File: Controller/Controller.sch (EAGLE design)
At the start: 40 parts, among them Q1 16Mhz, Q2 DMMT5401, Q3 DMG2305UX

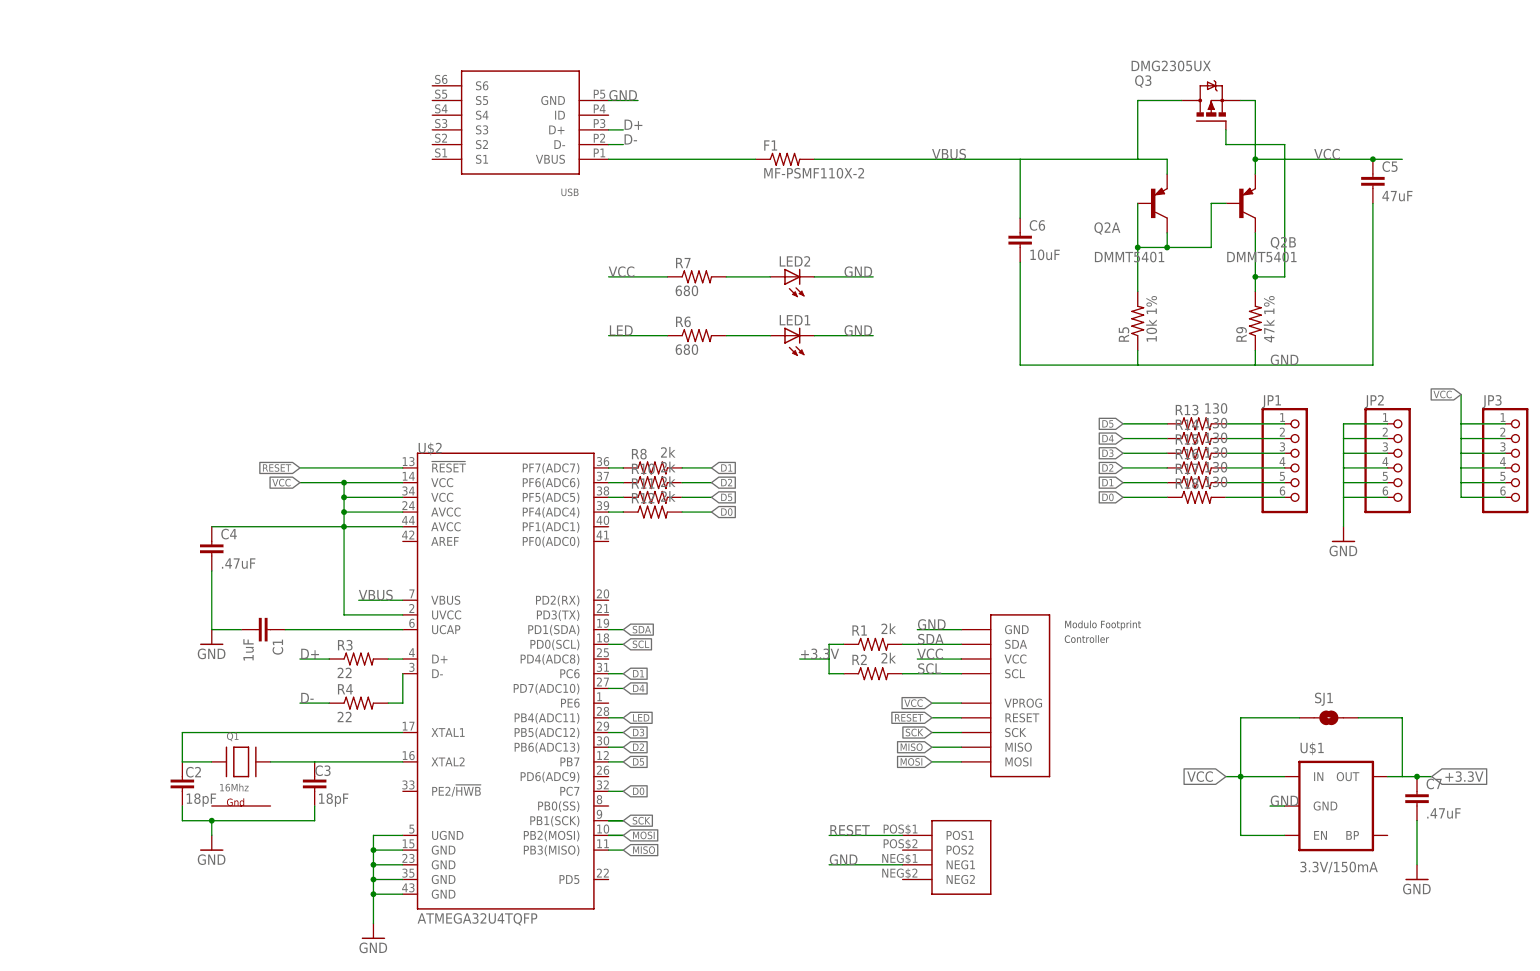
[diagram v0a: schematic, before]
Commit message: Renamed 32u4 to Controller
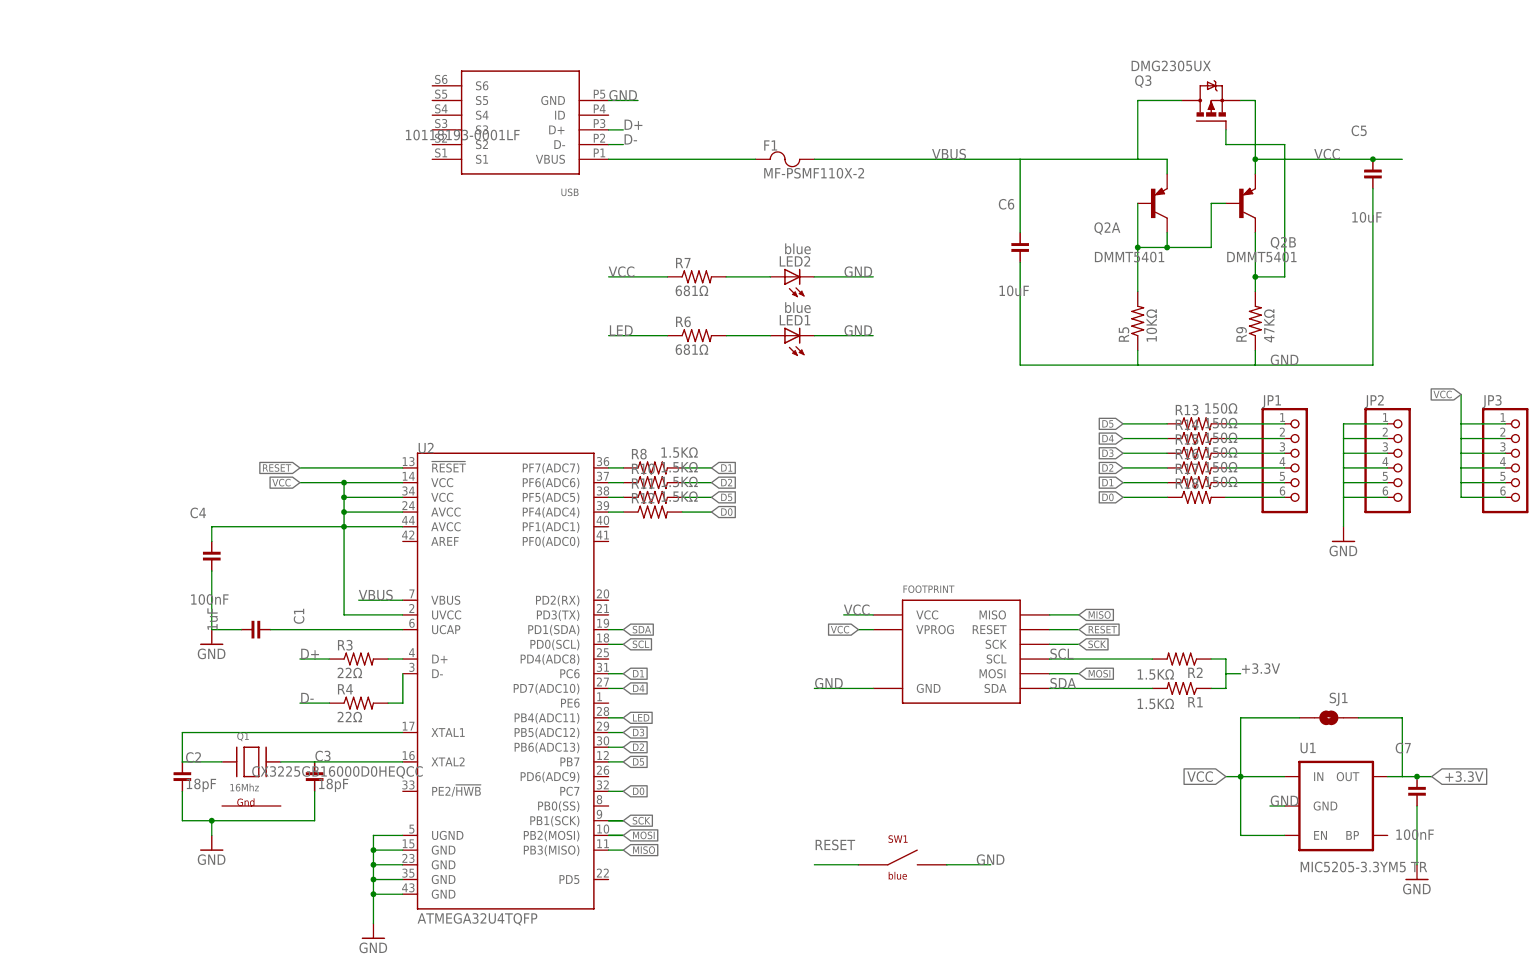
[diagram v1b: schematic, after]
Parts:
- removed U$1: 3.3V/150mA, SparkFun-PowerIC:V_REG_MIC52053.3V
- removed U$6: TACT-SWITCHBOURNS-7914J, IntegerLabs:TACT-SWITCHBOURNS-7914J
- added SW1: blue, Modulo:SWITCHBOURNS-7914J
- added U1: MIC5205-3.3YM5 TR, Modulo:VREG-MIC5205-3.3V
- C1: device SparkFun-Capacitors:CAP0805 -> Modulo:CAPACITOR-1UF
- C2, C3: device SparkFun-Capacitors:CAP0805 -> Modulo:CAPACITOR-18PF
- C4, C7: value .47uF -> 100nF; device SparkFun-Capacitors:CAP0805 -> Modulo:CAPACITOR-100NF
- C5: value 47uF -> 10uF; device SparkFun-Capacitors:CAP1206 -> Modulo:CAPACITOR-10UF
- C6: device SparkFun-Capacitors:CAP0805 -> Modulo:CAPACITOR-10UF
- F1: device SparkFun-Resistors:RESISTOR0805-RES -> Modulo:FUSE; PARTNUM (none) -> MF-PSFM110X-2
- FOOTPRINT: value Controller -> DEVICE-PCB-TABS; device IntegerLabs:FOOTPRINTFOOTPRINT-2 -> Modulo:DEVICE-PCB-TABS; BOARD Controller -> (none); VERSION v5 -> (none)
- JP1, JP2, JP3: PARTNUM (none) -> PREC006SAAN-RC
- LED1: value (none) -> blue; device adafruit:LEDCHIP-LED0805 -> Modulo:LED-0805-BLUE
- LED2: value (none) -> blue; device led:LEDCHIPLED_0805 -> Modulo:LED-0805-BLUE
- Q1: device adafruit:XTAL-4-3225 -> Modulo:CRYSTAL-NX3225; PARTNUM (none) -> CX3225GB16000D0HEQCC
- Q2: PARTNUM (none) -> DMMT5401
- Q3: PARTNUM (none) -> DMG2305UX
- R1, R10, R11, R12, R2, R8: value 2k -> 1.5KΩ; device SparkFun-Resistors:RESISTOR0805-RES -> Modulo:RESISTOR-1.5KΩ
- R13, R14, R15, R16, R17, R18: value 130 -> 150Ω; device SparkFun-Resistors:RESISTOR0805-RES -> Modulo:RESISTOR-150Ω
- R3, R4: value 22 -> 22Ω; device SparkFun-Resistors:RESISTOR0805-RES -> Modulo:RESISTOR-22Ω
- R5: value 10k 1% -> 10KΩ; device SparkFun-Passives:RESISTOR0805-RES -> Modulo:RESISTOR-10KΩ
- R6, R7: value 680 -> 681Ω; device SparkFun-Resistors:RESISTOR0805-RES -> Modulo:RESISTOR-681Ω
- R9: value 47k 1% -> 47KΩ; device SparkFun-Passives:RESISTOR0805-RES -> Modulo:RESISTOR-47KΩ
- SJ1: PARTNUM (none) -> EXCLUDE
- U2: PARTNUM (none) -> ATMEGA32U4TQFP
- U3: PARTNUM (none) -> 10118193-0001LF
- renumbered U$2 to U2, U$4 to U3
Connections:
- net +3.3V: now also U1.OUT; no longer U$1.OUT
- net GND: now also SW1.NEG1, U1.GND; no longer U$1.GND, U$6.NEG1
- net RESET: now also SW1.POS1; no longer U$6.POS1
- net VCC: now also U1.EN, U1.IN; no longer U$1.EN, U$1.IN
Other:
- moved on the sheet: Q1, R1, R2

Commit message: Major revision of all boards. Cleaned up old files. Exported BOM csv files for all boards
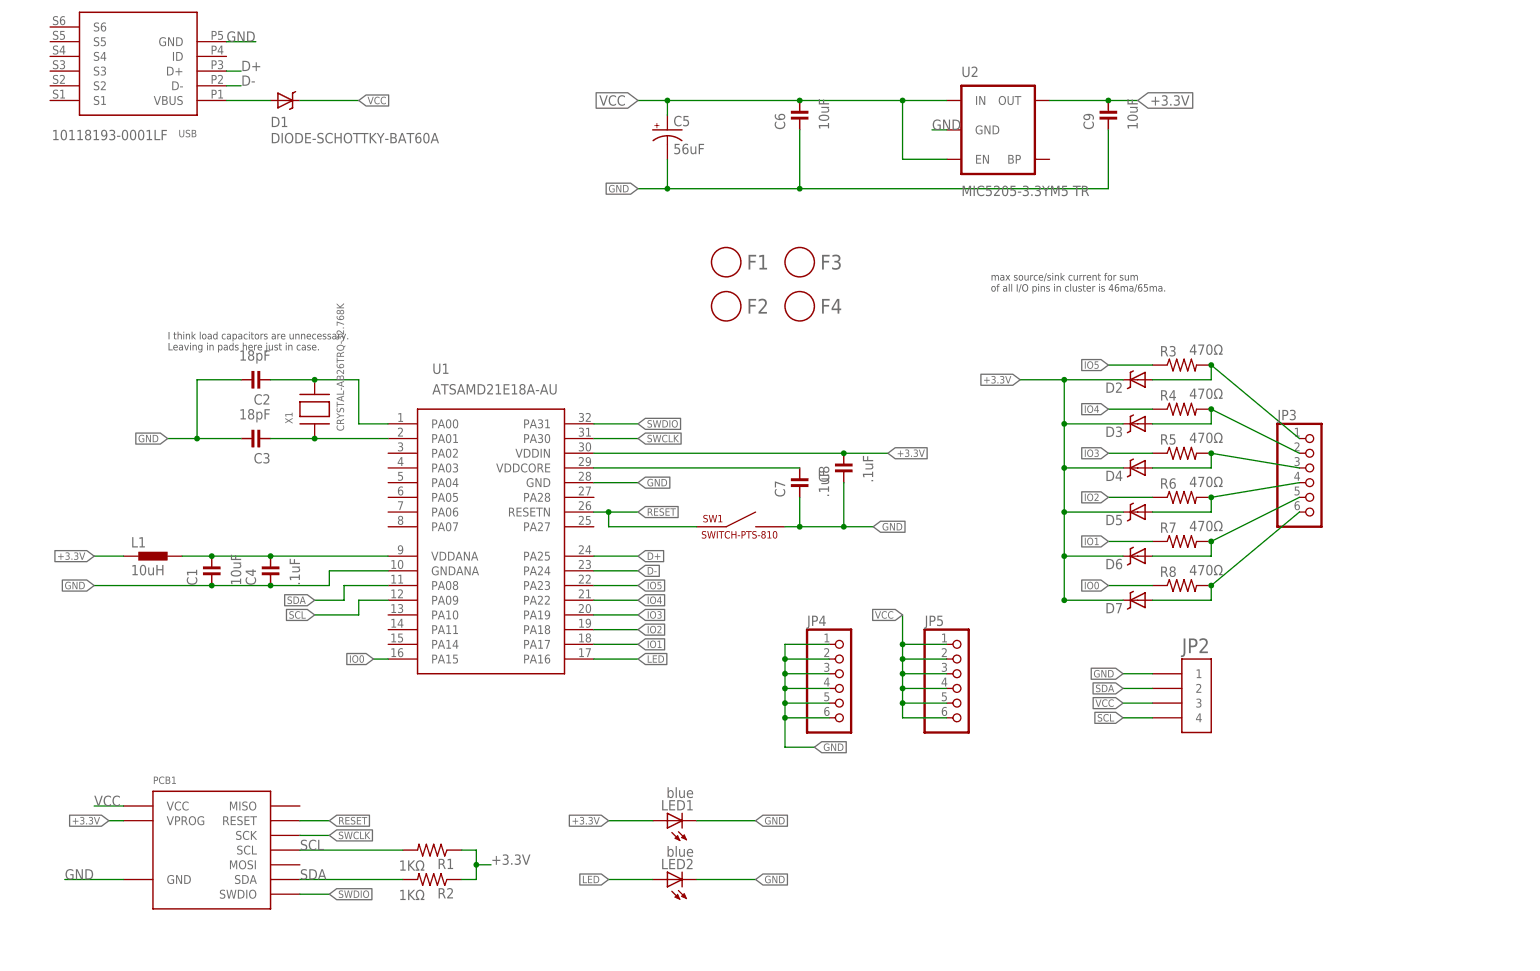
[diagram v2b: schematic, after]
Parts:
- removed FOOTPRINT: DEVICE-PCB-TABS, Modulo:DEVICE-PCB-TABS
- removed Q1: 16Mhz, Modulo:CRYSTAL-NX3225
- removed Q2: DMMT5401, IntegerLabs:TRANSISTOR-DUAL-PNP
- removed Q3: DMG2305UX, transistor-power:IRLML5203
- removed R10, R11, R12: 1.5KΩ, Modulo:RESISTOR-1.5KΩ
- removed R13, R14, R15, R16, R17, R18: 150Ω, Modulo:RESISTOR-150Ω
- removed R9: 47KΩ, Modulo:RESISTOR-47KΩ
- removed SJ1: SOLDERJUMPERNO, SparkFun-Passives:SOLDERJUMPERNO
- removed U3: USBFCI-MICROB, IntegerLabs:USBFCI-MICROB
- added C8: .1uF, Modulo:CAPACITOR-.1UF
- added C9: 10uF, Modulo:CAPACITOR-10UF
- added D1, D2, D3, D4, D5, D6, D7: DIODE-SCHOTTKY-BAT60A, Modulo:DIODE-SCHOTTKY-BAT60A
- added F2, F3, F4: FIDUCIAL, Modulo:FIDUCIAL
- added JP4, JP5: (no value), adafruit:PINHD-1X6LOCK
- added L1: 10uH, Modulo:INDUCTOR-10UH
- added PCB1: DEVICE-PCB, Modulo:DEVICE-PCB
- added X1: CRYSTAL-AB26TRQ-32.768K, Modulo:CRYSTAL-AB26TRQ-32.768K
- C1: value 1uF -> 10uF; device Modulo:CAPACITOR-1UF -> Modulo:CAPACITOR-10UF
- C2, C3: BOM (none) -> EXCLUDE
- C4, C7: value 100nF -> .1uF; device Modulo:CAPACITOR-100NF -> Modulo:CAPACITOR-.1UF
- C5: value 10uF -> 56uF; device Modulo:CAPACITOR-10UF -> Modulo:CAPACITOR-POL-56UF-25V
- F1: value MF-PSMF110X-2 -> FIDUCIAL; device Modulo:FUSE -> Modulo:FIDUCIAL; PARTNUM MF-PSFM110X-2 -> (none)
- JP1: value (none) -> USBFCI-MICROB; device adafruit:PINHD-1X6LOCK -> Modulo:USBFCI-MICROB; PARTNUM PREC006SAAN-RC -> 10118193-0001LF
- JP2: value (none) -> HEADER-1X4-AMPMODU; device adafruit:PINHD-1X6LOCK -> Modulo:HEADER-1X4-AMPMODU; PARTNUM PREC006SAAN-RC -> (none)
- R1, R2: value 1.5KΩ -> 1KΩ; device Modulo:RESISTOR-1.5KΩ -> Modulo:RESISTOR-1KΩ
- R3, R4: value 22Ω -> 470Ω; device Modulo:RESISTOR-22Ω -> Modulo:RESISTOR-470Ω
- R5: value 10KΩ -> 470Ω; device Modulo:RESISTOR-10KΩ -> Modulo:RESISTOR-470Ω
- R6, R7: value 681Ω -> 470Ω; device Modulo:RESISTOR-681Ω -> Modulo:RESISTOR-470Ω
- R8: value 1.5KΩ -> 470Ω; device Modulo:RESISTOR-1.5KΩ -> Modulo:RESISTOR-470Ω
- SW1: value blue -> SWITCH-PTS-810; device Modulo:SWITCHBOURNS-7914J -> Modulo:SWITCH-PTS-810
- U1: value MIC5205-3.3YM5 TR -> ATSAMD21E18A-AU; device Modulo:VREG-MIC5205-3.3V -> Modulo:SAMD21E; PARTNUM MIC5205-3.3YM5 TR -> ATSAMD21E18A-AU
- U2: value ATMEGA32U4TQFP -> MIC5205-3.3YM5 TR; device SparkFun-DigitalIC:ATMEGA32U4TQFP -> Modulo:VREG-MIC5205-3.3V; PARTNUM ATMEGA32U4TQFP -> MIC5205-3.3YM5
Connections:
- removed net D0: R12.2, R18.1, U2.PC7
- removed net D1: R17.1, R8.2, U2.PC6
- removed net D2: R10.2, R16.1, U2.PB6(ADC13)
- removed net D3: R15.1, U2.PB5(ADC12)
- removed net D4: R14.1, U2.PD7(ADC10)
- removed net D5: R11.2, R13.1, U2.PB7
- removed net MISO: FOOTPRINT.MISO, U2.PB3(MISO)
- removed net MOSI: FOOTPRINT.MOSI, U2.PB2(MOSI)
- removed net N$1: C1.1, U2.UCAP
- removed net N$10: R10.1, U2.PF6(ADC6)
- removed net N$11: R8.1, U2.PF7(ADC7)
- removed net N$12: LED2.A, R7.2
- removed net N$14: Q2A.B, Q2A.C, Q2B.B, R5.2
- removed net N$15: C2.1, Q1.X1, U2.XTAL1
- removed net N$16: Q2B.C, Q3.G, R9.2
- removed net N$4: C3.1, Q1.X2, U2.XTAL2
- removed net N$5: LED1.A, R6.2
- removed net N$8: R3.2, U2.D+
- removed net N$9: R4.2, U2.D-
- removed net SCK: FOOTPRINT.SCK, U2.PB1(SCK)
- removed net VBUS: C6.1, F1.2, Q2A.E, Q3.D, U2.VBUS
- new net IO0: R8.1, U1.PA15
- new net IO1: R7.1, U1.PA17
- new net IO2: R6.1, U1.PA18
- new net IO3: R5.1, U1.PA19
- new net IO4: R4.1, U1.PA22
- new net IO5: R3.1, U1.PA23
- new net N$21: C1.1, C4.1, L1.2, U1.VDDANA
- new net N$22: C7.1, U1.VDDCORE
- new net SWCLK: PCB1.SCK, U1.PA30
- new net SWDIO: PCB1.SWDIO, U1.PA31
- net +3.3V: now also C8.1, C9.1, D2.C, D3.C, D4.C, D5.C, D6.C, D7.C, L1.1, LED1.A, PCB1.VPROG, U1.VDDIN, U2.OUT; no longer C7.1, SJ1.2, U1.OUT
- net D+: now also JP1.D+, U1.PA25; no longer R3.1, U3.D+
- net D-: now also JP1.D-, U1.PA24; no longer R4.1, U3.D-
- net GND: now also C2.1, C3.1, C5.-, C8.2, C9.2, JP1.GND, JP4.1, JP4.2, JP4.3, JP4.4, JP4.5, JP4.6, PCB1.GND, U1.GNDANA, U2.GND; no longer C2.2, C3.2, C5.2, FOOTPRINT.GND, JP2.2, JP2.3, JP2.4, JP2.5, JP2.6, R5.1, R9.1, U2.GND@15, U2.GND@23, U2.GND@35, U2.GND@43, U2.UGND, U3.GND
- net LED: now also LED2.A, U1.PA16; no longer R6.1, U2.PB4(ADC11)
- net N$13: now also D3.A, JP3.2, R4.2; no longer JP1.2, R14.2
- net N$17: now also D4.A, JP3.3, R5.2; no longer JP1.3, R15.2
- net N$18: now also D5.A, JP3.4, R6.2; no longer JP1.4, R16.2
- net N$19: now also D6.A, JP3.5, R7.2; no longer JP1.5, R17.2
- net N$2: now also D2.A, JP3.1, R3.2; no longer JP1.1, R13.2
- net N$20: now also D7.A, JP3.6, R8.2; no longer JP1.6, R18.2
- net N$3: now also D1.A, JP1.VBUS; no longer F1.1, U3.VBUS
- net N$6: now also C2.2, U1.PA00, X1.X2; no longer R12.1, U2.PF4(ADC4)
- net N$7: now also C3.2, U1.PA01, X1.X1; no longer R11.1, U2.PF5(ADC5)
- net RESET: now also PCB1.RESET, U1.RESETN; no longer FOOTPRINT.RESET, U2.!RESET
- net SCL: now also JP2.4, PCB1.SCL, R1.2, U1.PA09; no longer FOOTPRINT.SCL, R2.2, U2.PD0(SCL)
- net SDA: now also JP2.2, PCB1.SDA, R2.2, U1.PA08; no longer FOOTPRINT.SDA, R1.2, U2.PD1(SDA)
- net VCC: now also C5.+, C6.1, D1.C, JP2.3, JP5.1, JP5.2, JP5.3, JP5.4, JP5.5, JP5.6, PCB1.VCC, U2.EN, U2.IN; no longer C4.1, C5.1, FOOTPRINT.VCC, FOOTPRINT.VPROG, JP3.1, JP3.2, JP3.3, JP3.4, JP3.5, JP3.6, Q2B.E, Q3.S, R7.1, SJ1.1, U1.EN, U1.IN, U2.AVCC@24, U2.AVCC@44, U2.UVCC, U2.VCC@14, U2.VCC@34
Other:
- note added: "I think load capacitors are unnecessary. Leaving in pads here just in case."
- note added: "max source/sink current for sum of all I/O pins in cluster is 46ma/65ma."
- moved on the sheet: C1, C2, C3, C4, C6, C7, JP3, LED1, LED2, R1, R2, R3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

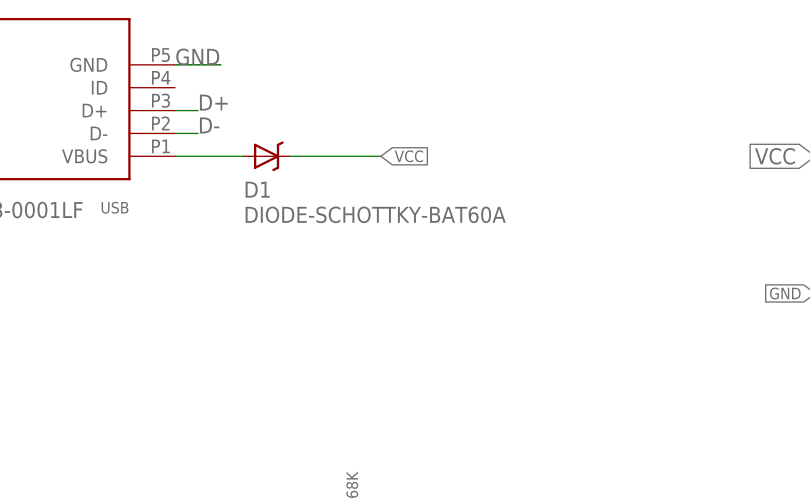
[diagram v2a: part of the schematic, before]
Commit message: New diode selections
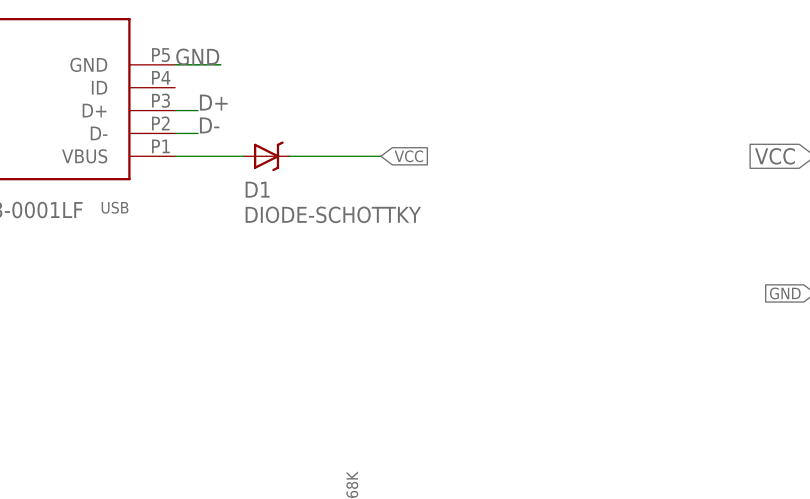
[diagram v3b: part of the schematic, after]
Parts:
- D1: value DIODE-SCHOTTKY-BAT60A -> DIODE-SCHOTTKY; device Modulo:DIODE-SCHOTTKY-BAT60A -> Modulo:DIODE-SCHOTTKY
- D2, D3, D4, D5, D6, D7: PARTNUM (none) -> CUS520,H3F
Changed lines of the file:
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@@
 </part>
 <part name="JP2" library="Modulo" deviceset="HEADER-1X4" device="-AMPMODU"/>
-<part name="D2" library="Modulo" deviceset="DIODE-SCHOTTKY" device="-BAT60A"/>
-<part name="D3" library="Modulo" deviceset="DIODE-SCHOTTKY" device="-BAT60A"/>
-<part name="D4" library="Modulo" deviceset="DIODE-SCHOTTKY" device="-BAT60A"/>
-<part name="D5" library="Modulo" deviceset="DIODE-SCHOTTKY" device="-BAT60A"/>
-<part name="D6" library="Modulo" deviceset="DIODE-SCHOTTKY" device="-BAT60A"/>
-<part name="D7" library="Modulo" deviceset="DIODE-SCHOTTKY" device="-BAT60A"/>
-<part name="D1" library="Modulo" deviceset="DIODE-SCHOTTKY" device="-BAT60A"/>
+<part name="D2" library="Modulo" deviceset="DIODE-SCHOTTKY" device="-BAT60A">
+<attribute name="PARTNUM" value="CUS520,H3F"/>
+</part>
+<part name="D3" library="Modulo" deviceset="DIODE-SCHOTTKY" device="-BAT60A">
+<attribute name="PARTNUM" value="CUS520,H3F"/>
+</part>
+<part name="D4" library="Modulo" deviceset="DIODE-SCHOTTKY" device="-BAT60A">
+<attribute name="PARTNUM" value="CUS520,H3F"/>
+</part>
+<part name="D5" library="Modulo" deviceset="DIODE-SCHOTTKY" device="-BAT60A">
+<attribute name="PARTNUM" value="CUS520,H3F"/>
+</part>
+<part name="D6" library="Modulo" deviceset="DIODE-SCHOTTKY" device="-BAT60A">
+<attribute name="PARTNUM" value="CUS520,H3F"/>
+</part>
+<part name="D7" library="Modulo" deviceset="DIODE-SCHOTTKY" device="-BAT60A">
+<attribute name="PARTNUM" value="CUS520,H3F"/>
+</part>
+<part name="D1" library="Modulo" deviceset="DIODE-SCHOTTKY" device="" value="DIODE-SCHOTTKY"/>
 <part name="C5" library="Modulo" deviceset="CAPACITOR-POL" device="-56UF-25V" value="56uF"/>
 <part name="SW1" library="Modulo" deviceset="SWITCH" device="-PTS-810"/>
